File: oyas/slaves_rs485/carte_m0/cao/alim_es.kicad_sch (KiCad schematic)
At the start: 50 parts, among them J1 POWER, U1 BPC_Alim5V, U1 MAX3485, U4 AP1117-15

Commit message: Finitions PCB
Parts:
- D9: footprint Package_TO_SOT_SMD:SOT-23 -> bpc:BPC_SOT-23-3_HandSoldering
- Q?: footprint bpc:BPC_SOT-23-3 -> bpc:BPC_SOT-23-3_HandSoldering
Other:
- company: (none) -> BPC
- title: (none) -> Carte Oya M0
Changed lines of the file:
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@@
 (kicad_sch (version 20230121) (generator eeschema)
   (paper "A4")
+  (title_block
+    (title "Carte Oya M0")
+    (date "2026-03-06")
+    (rev "Rev A")
+    (company "BPC")
+  )
   (junction (at 179.07 34.29) (diameter 0) (color 0 0 0 0)
   )
@@
       (effects (font (size 1.27 1.27)) (justify left))
     )
-    (property "Footprint" "Package_TO_SOT_SMD:SOT-23" (at 245.11 63.5 0)
+    (property "Footprint" "bpc:BPC_SOT-23-3_HandSoldering" (at 245.11 63.5 0)
       (effects (font (size 1.27 1.27)) hide)
     )
@@
       (effects (font (size 1.27 1.27)) (justify left))
     )
-    (property "Footprint" "bpc:BPC_SOT-23-3" (at 237.49 130.81 0)
-      (effects (font (size 1.27 1.27)) hide)
-    )
+    (property "Footprint" "bpc:BPC_SOT-23-3_HandSoldering" (at 237.49 130.81 0)
+      (effects (font (size 1.27 1.27)) hide)
+    )

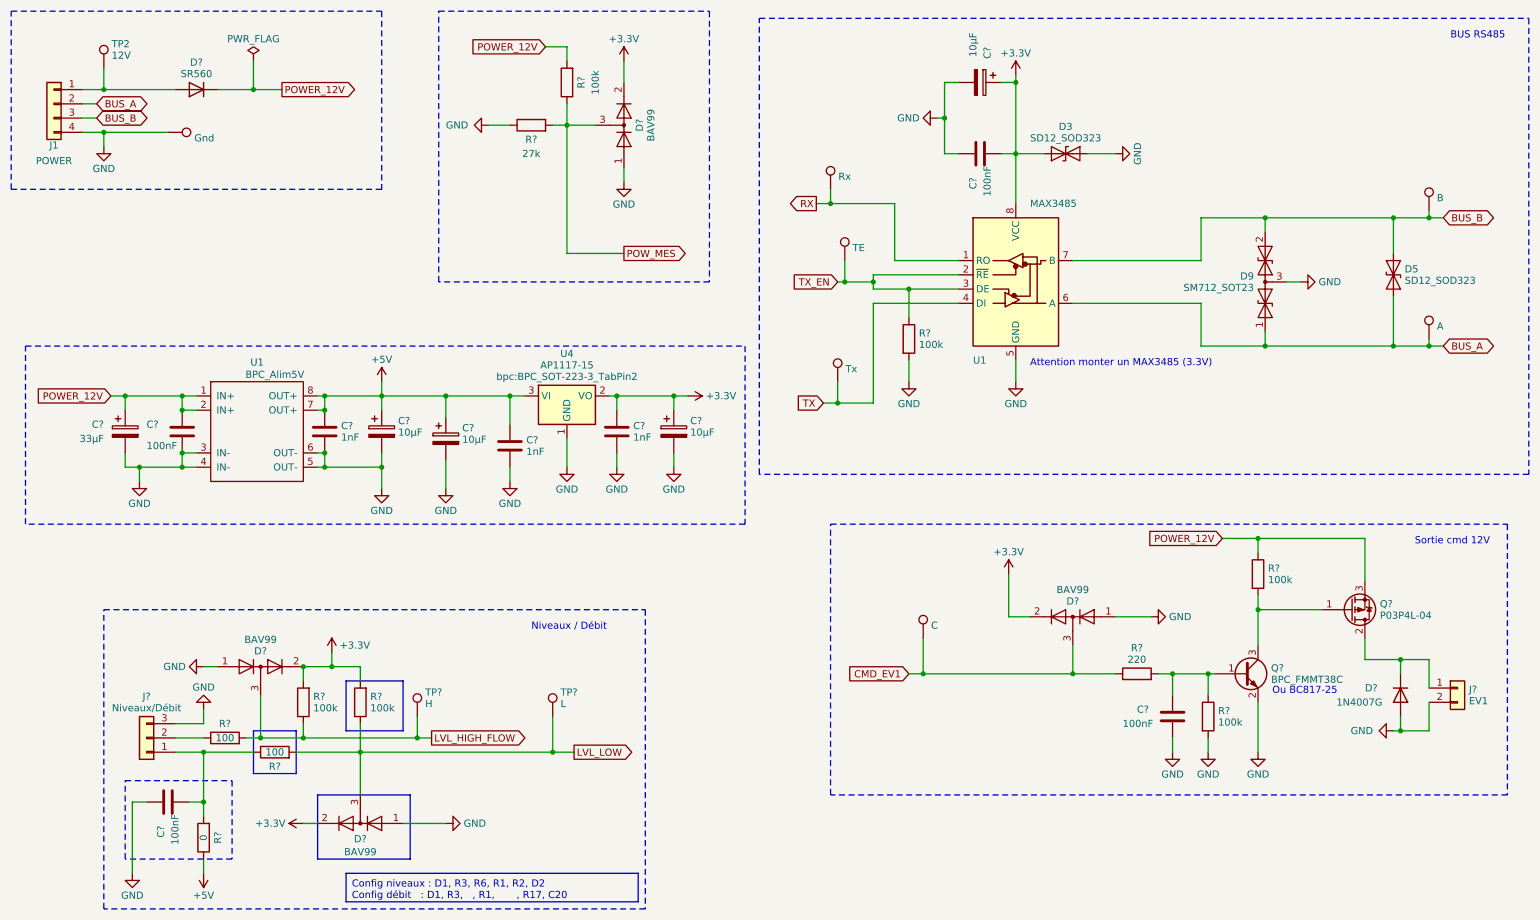
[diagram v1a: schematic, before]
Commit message: Revue de carte et de routage:
- Amélioration découplage micro (1uF 805 sur VDDCore et 100nF 603 sur les autres selon recommendation microchip)
- R14=1k: Moins de courant dans Q1
- R1=R2=1k: Limiter le clamp en mode débit
- R3 NM en mode débit
- C17=100nF pour améliorer filtrage 3.3V
- Ajout Capa 100nF sur reset
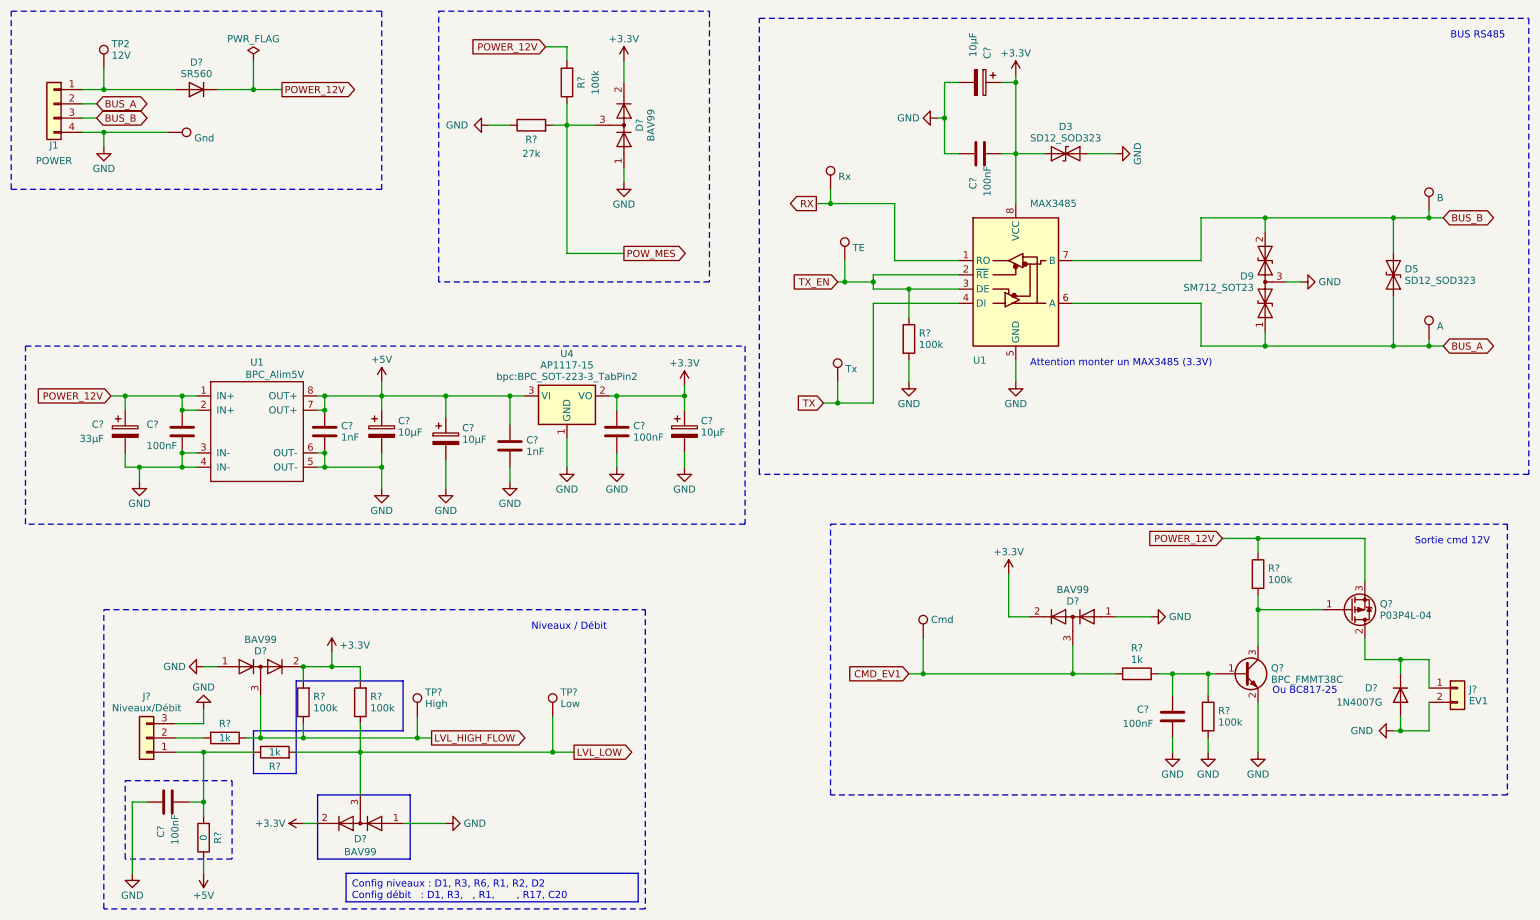
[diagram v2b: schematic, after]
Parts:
- C?: value 1nF -> 100nF
- R? (x2): value 100 -> 1k
- R?: value 220 -> 1k
- TP?: value L -> Low
- TP?: value C -> Cmd
- TP?: value H -> High
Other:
- moved on the sheet: C?
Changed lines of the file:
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@@
   (junction (at 260.35 130.81) (diameter 0) (color 0 0 0 0)
   )
-  (junction (at 130.81 83.82) (diameter 0) (color 0 0 0 0)
-  )
   (junction (at 265.43 52.07) (diameter 0) (color 0 0 0 0)
   )
@@
   (junction (at 109.22 147.32) (diameter 0) (color 0 0 0 0)
   )
+  (junction (at 132.715 83.82) (diameter 0) (color 0 0 0 0)
+  )
   (junction (at 219.71 133.35) (diameter 0) (color 0 0 0 0)
   )
@@
     (stroke (width 0) (type default))
   )
+  (wire (pts (xy 132.715 81.915) (xy 132.715 83.82))
+    (stroke (width 0) (type default))
+  )
   (wire (pts (xy 228.6 109.22) (xy 234.95 109.22))
     (stroke (width 0) (type default))
@@
     (stroke (width 0) (type default))
   )
-  (wire (pts (xy 120.65 83.82) (xy 130.81 83.82))
+  (wire (pts (xy 120.65 83.82) (xy 132.715 83.82))
     (stroke (width 0) (type default))
   )
@@
     (stroke (width 0) (type default))
   )
-  (wire (pts (xy 130.81 93.98) (xy 130.81 96.52))
+  (wire (pts (xy 132.715 93.98) (xy 132.715 96.52))
     (stroke (width 0) (type default))
   )
@@
     (stroke (width 0) (type default))
   )
-  (wire (pts (xy 130.81 83.82) (xy 133.35 83.82))
-    (stroke (width 0) (type default))
-  )
   (wire (pts (xy 85.09 144.78) (xy 87.63 144.78))
     (stroke (width 0) (type default))
@@
     (stroke (width 0) (type default))
   )
-  (wire (pts (xy 130.81 83.82) (xy 130.81 86.36))
+  (wire (pts (xy 132.715 83.82) (xy 132.715 86.36))
     (stroke (width 0) (type default))
   )
@@
     (fill (type none))
   )
-  (rectangle (start 72.39 134.62) (end 82.55 143.51)
+  (rectangle (start 63.5 134.62) (end 82.55 143.51)
     (stroke (width 0) (type solid))
     (fill (type none))
@@
       (effects (font (size 1.27 1.27)) (justify left))
     )
-    (property "Value" "L" (at 110.617 138.692 0)
+    (property "Value" "Low" (at 110.617 138.692 0)
       (effects (font (size 1.27 1.27)) (justify left))
     )
@@
       (effects (font (size 1.27 1.27)))
     )
-    (property "Value" "100" (at 50.8 144.78 90)
+    (property "Value" "1k" (at 50.8 144.78 90)
       (effects (font (size 1.27 1.27)))
     )
@@
       (effects (font (size 1.27 1.27)) (justify left))
     )
-    (property "Value" "1nF" (at 123.571 91.194 0)
+    (property "Value" "100nF" (at 123.571 91.194 0)
       (effects (font (size 1.27 1.27)) (justify left))
     )
@@
     )
   )
-  (symbol (lib_id "power:GND") (at 130.81 96.52 0) (unit 1)
+  (symbol (lib_id "power:GND") (at 132.715 96.52 0) (unit 1)
     (in_bom yes) (on_board yes) (dnp no) (fields_autoplaced)
-    (property "Reference" "#PWR?" (at 130.81 102.87 0)
+    (property "Reference" "#PWR?" (at 132.715 102.87 0)
       (effects (font (size 1.27 1.27)) hide)
     )
-    (property "Value" "GND" (at 130.81 100.465 0)
+    (property "Value" "GND" (at 132.715 100.465 0)
       (effects (font (size 1.27 1.27)))
     )
-    (property "Footprint" "" (at 130.81 96.52 0)
+    (property "Footprint" "" (at 132.715 96.52 0)
       (effects (font (size 1.27 1.27)) hide)
     )
-    (property "Datasheet" "" (at 130.81 96.52 0)
+    (property "Datasheet" "" (at 132.715 96.52 0)
       (effects (font (size 1.27 1.27)) hide)
     )
@@
       (effects (font (size 1.27 1.27)) (justify left) hide)
     )
-    (property "Value" "C" (at 176.657 124.722 0)
+    (property "Value" "Cmd" (at 176.657 123.698 0)
       (effects (font (size 1.27 1.27)) (justify left))
     )
@@
       (effects (font (size 1.27 1.27)) (justify left))
     )
-    (property "Value" "H" (at 86.487 138.692 0)
+    (property "Value" "High" (at 86.487 138.692 0)
       (effects (font (size 1.27 1.27)) (justify left))
     )
@@
       (effects (font (size 1.27 1.27)))
     )
-    (property "Value" "100" (at 59.69 147.32 90)
+    (property "Value" "1k" (at 59.69 147.32 90)
       (effects (font (size 1.27 1.27)))
     )
@@
     )
   )
-  (symbol (lib_id "power:+3.3V") (at 133.35 83.82 270) (unit 1)
+  (symbol (lib_id "power:+3.3V") (at 132.715 81.915 0) (unit 1)
     (in_bom yes) (on_board yes) (dnp no) (fields_autoplaced)
-    (property "Reference" "#PWR025" (at 129.54 83.82 0)
+    (property "Reference" "#PWR025" (at 132.715 85.725 0)
       (effects (font (size 1.27 1.27)) hide)
     )
-    (property "Value" "+3.3V" (at 136.525 83.82 90)
-      (effects (font (size 1.27 1.27)) (justify left))
+    (property "Value" "+3.3V" (at 132.715 77.97 0)
+      (effects (font (size 1.27 1.27)))
     )
-    (property "Footprint" "" (at 133.35 83.82 0)
+    (property "Footprint" "" (at 132.715 81.915 0)
       (effects (font (size 1.27 1.27)) hide)
     )
-    (property "Datasheet" "" (at 133.35 83.82 0)
+    (property "Datasheet" "" (at 132.715 81.915 0)
       (effects (font (size 1.27 1.27)) hide)
     )
@@
     )
   )
-  (symbol (lib_id "Device:C_Polarized") (at 130.81 90.17 0) (unit 1)
+  (symbol (lib_id "Device:C_Polarized") (at 132.715 90.17 0) (unit 1)
     (in_bom yes) (on_board yes) (dnp no) (fields_autoplaced)
-    (property "Reference" "C?" (at 133.731 88.257 0)
+    (property "Reference" "C?" (at 135.636 88.257 0)
       (effects (font (size 1.27 1.27)) (justify left))
     )
-    (property "Value" "10µF" (at 133.731 90.305 0)
+    (property "Value" "10µF" (at 135.636 90.305 0)
       (effects (font (size 1.27 1.27)) (justify left))
     )
-    (property "Footprint" "Capacitor_SMD:CP_Elec_4x5.4" (at 131.7752 93.98 0)
+    (property "Footprint" "Capacitor_SMD:CP_Elec_4x5.4" (at 133.6802 93.98 0)
       (effects (font (size 1.27 1.27)) hide)
     )
-    (property "Datasheet" "~" (at 130.81 90.17 0)
+    (property "Datasheet" "~" (at 132.715 90.17 0)
       (effects (font (size 1.27 1.27)) hide)
     )
-    (property "Fabricant" "CHEMI-CON" (at 130.81 90.17 0)
+    (property "Fabricant" "CHEMI-CON" (at 132.715 90.17 0)
       (effects (font (size 1.27 1.27)) hide)
     )
-    (property "Fournisseur" "Farnell" (at 130.81 90.17 0)
+    (property "Fournisseur" "Farnell" (at 132.715 90.17 0)
       (effects (font (size 1.27 1.27)) hide)
     )
-    (property "RefFabricant" "EMZA350ADA100ME61G" (at 130.81 90.17 0)
+    (property "RefFabricant" "EMZA350ADA100ME61G" (at 132.715 90.17 0)
       (effects (font (size 1.27 1.27)) hide)
     )
-    (property "RefFournisseur" "1698723" (at 130.81 90.17 0)
+    (property "RefFournisseur" "1698723" (at 132.715 90.17 0)
       (effects (font (size 1.27 1.27)) hide)
     )
-    (property "Description" "Condensateur chimique 10µF" (at 130.81 90.17 0)
+    (property "Description" "Condensateur chimique 10µF" (at 132.715 90.17 0)
       (effects (font (size 1.27 1.27)) hide)
     )
-    (property "Price" "0,6312" (at 130.81 90.17 0)
+    (property "Price" "0,6312" (at 132.715 90.17 0)
       (effects (font (size 1.27 1.27)) hide)
     )
@@
       (effects (font (size 1.27 1.27)))
     )
-    (property "Value" "220" (at 213.36 130.802 90)
+    (property "Value" "1k" (at 213.36 130.802 90)
       (effects (font (size 1.27 1.27)))
     )
